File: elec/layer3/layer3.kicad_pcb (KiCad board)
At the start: 2 copper layers, 125 x 125 mm, 57 parts, among them J10 Conn_01x05, J4 Conn_01x05, J8 XT30PW-M, J9 XT30PW-M, SW1 SW_SPDT_312, SW2 SW_SPDT_312, SW3 SW_SPDT_312, SW4 SW_SPDT_312, U1 CD74HC4067SM, U2 CD74HC4067SM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

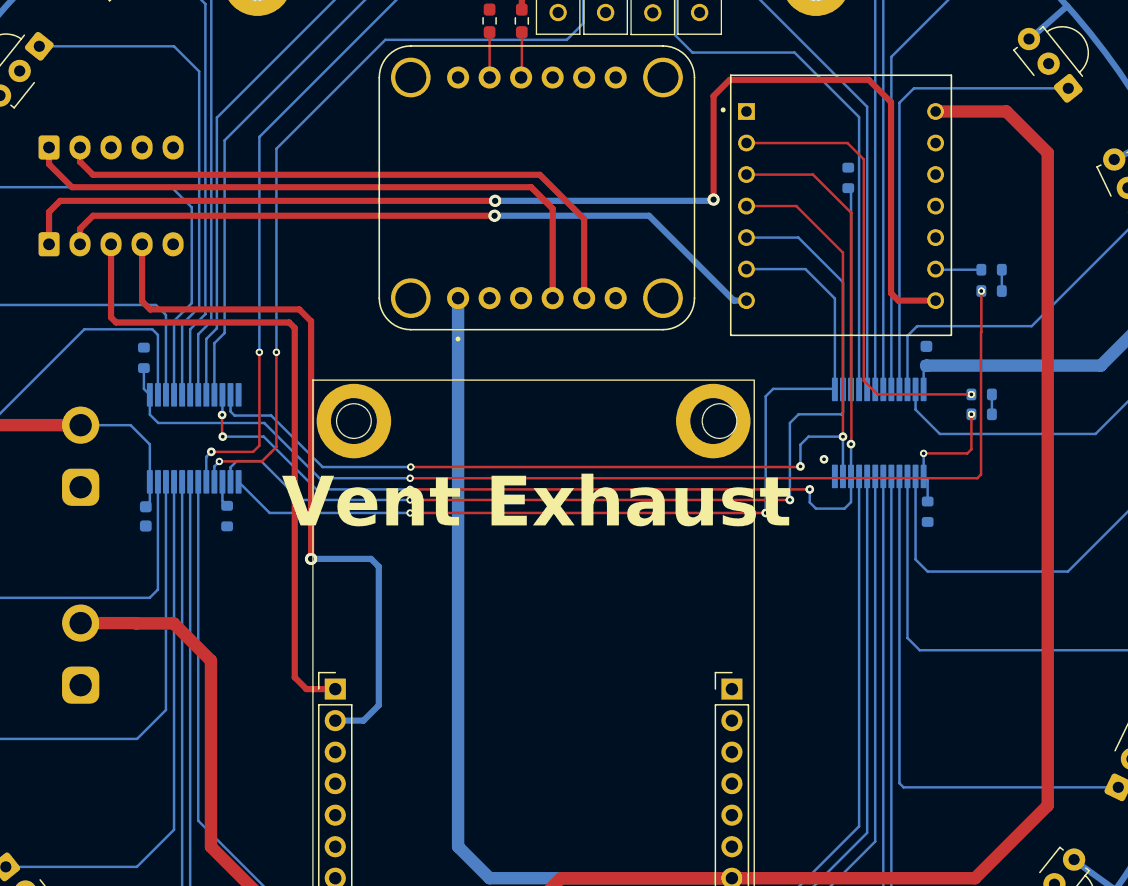
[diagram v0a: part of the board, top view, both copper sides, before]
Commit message: all layes drc and fixed
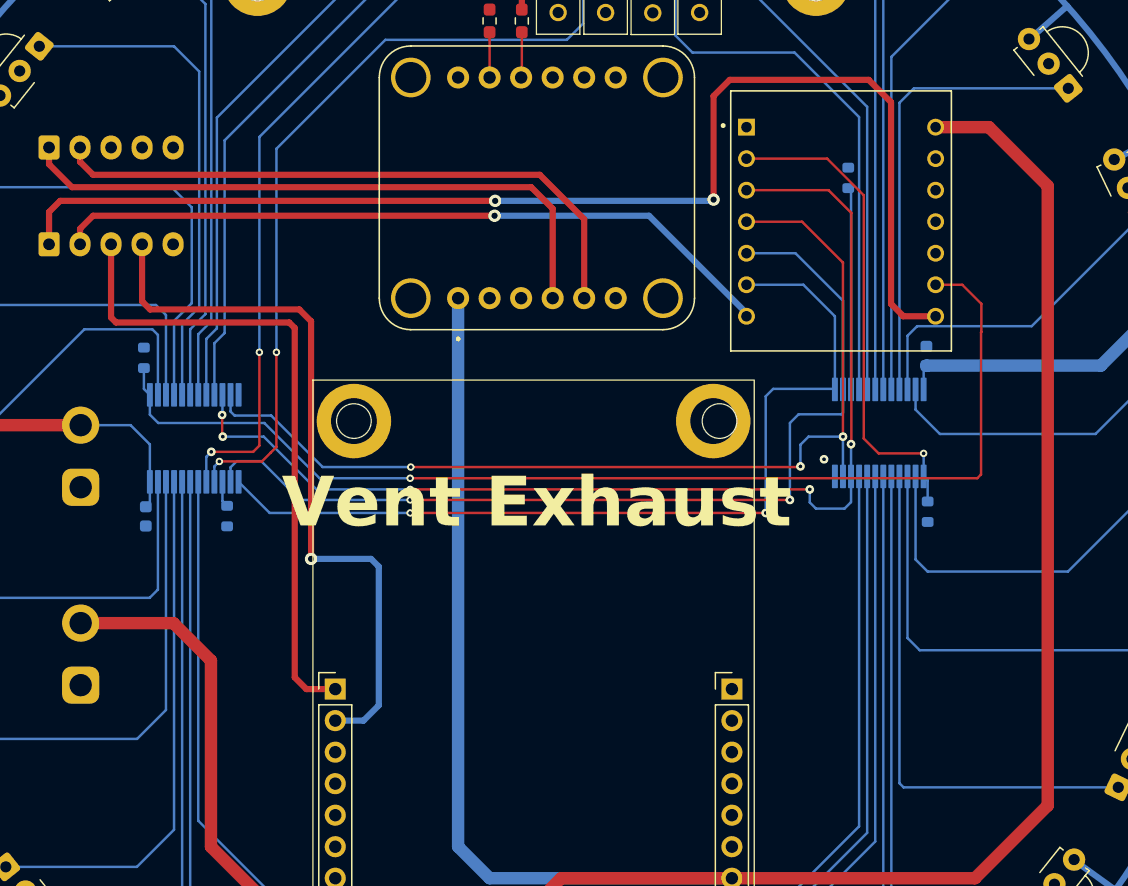
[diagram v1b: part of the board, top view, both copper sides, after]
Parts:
- removed R5, R7: 10k, Resistor_SMD:R_0603_1608Metric
- removed R6, R8: 10uF, Resistor_SMD:R_0603_1608Metric
- moved U5 1.26 mm to (171.1, 74.3)
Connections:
- U5 pad 2: Net-(U5-D1) -> /Mux Com (17-32)
- U5 pad 9: Net-(U5-D8) -> /Mux Com (1-16)
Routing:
- net Net-(U5-D1): track 37.0 -> 0.00 mm, vias 1 -> 0
- net /Mux Com (17-32): track 10.9 -> 39.7 mm, vias 2 -> 1
- net Net-(U5-D8): track 3.78 -> 0.00 mm
- net /Mux Com (1-16): track 88.0 -> 91.3 mm, vias 2 -> 1
- net +5V: track 235.4 -> 233.3 mm
- net Net-(R7-Pad2): track 1.72 -> 0.00 mm
- net Net-(R5-Pad2): track 1.60 -> 0.00 mm
- net /S2: track 78.3 -> 76.9 mm
- net /S3: track 74.2 -> 72.9 mm
- net /RX(ESP32): track 99.7 -> 100.8 mm
- net /S1: track 81.9 -> 81.0 mm
- net /TX(ESP32): track 58.2 -> 58.9 mm
- net /S0: track 90.4 -> 89.8 mm

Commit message: chore: fix all 3 layers; prod: all 3 layers
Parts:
- removed R1, R33: 3k24, Resistor_SMD:R_0603_1608Metric
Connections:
- U4 pad JP1_1: +5V -> +3V3
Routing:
- net +3V3: track 83.3 -> 151.2 mm
- net +5V: track 233.3 -> 166.0 mm
- net /Mux Com (1-16): track 91.3 -> 88.9 mm
- net /Mux Com (17-32): track 39.7 -> 37.5 mm
- net /IR1: track 58.9 -> 60.8 mm
